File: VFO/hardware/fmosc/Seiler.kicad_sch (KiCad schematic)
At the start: 32 parts, among them J2 U.FL, J3 JST PH, J4 3670128, Q1 MMBT5179, Q2 MMBT5179, Q3 MMBT5179, Q4 MMBT5179

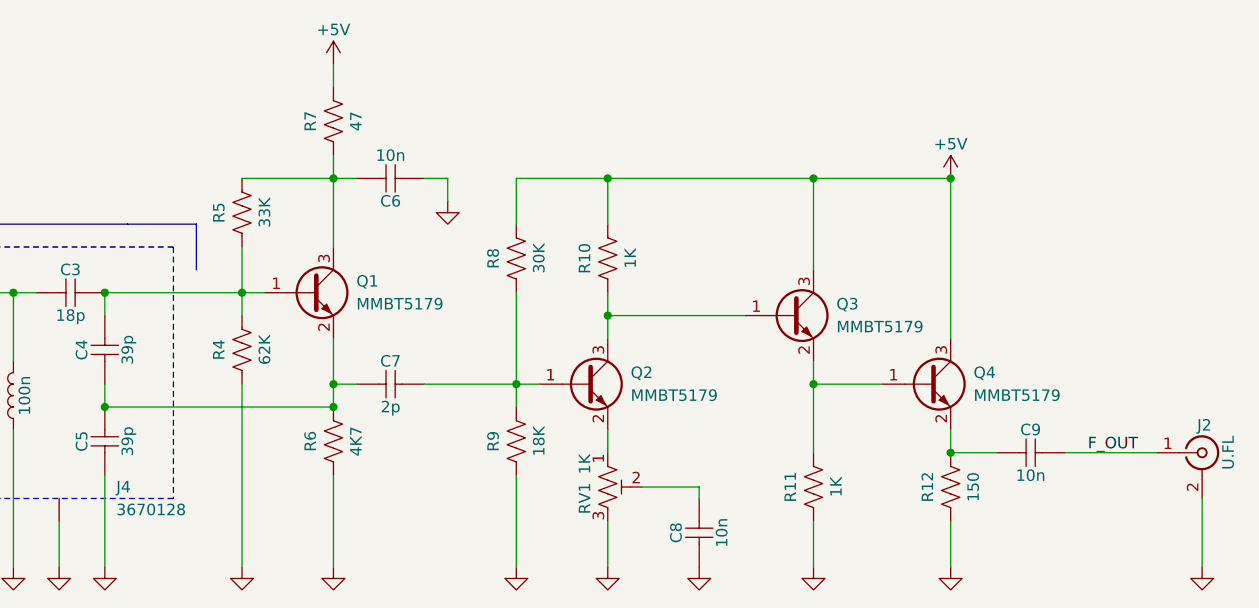
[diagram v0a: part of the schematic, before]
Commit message: Adding DC voltages to the schematic + updating from libraries
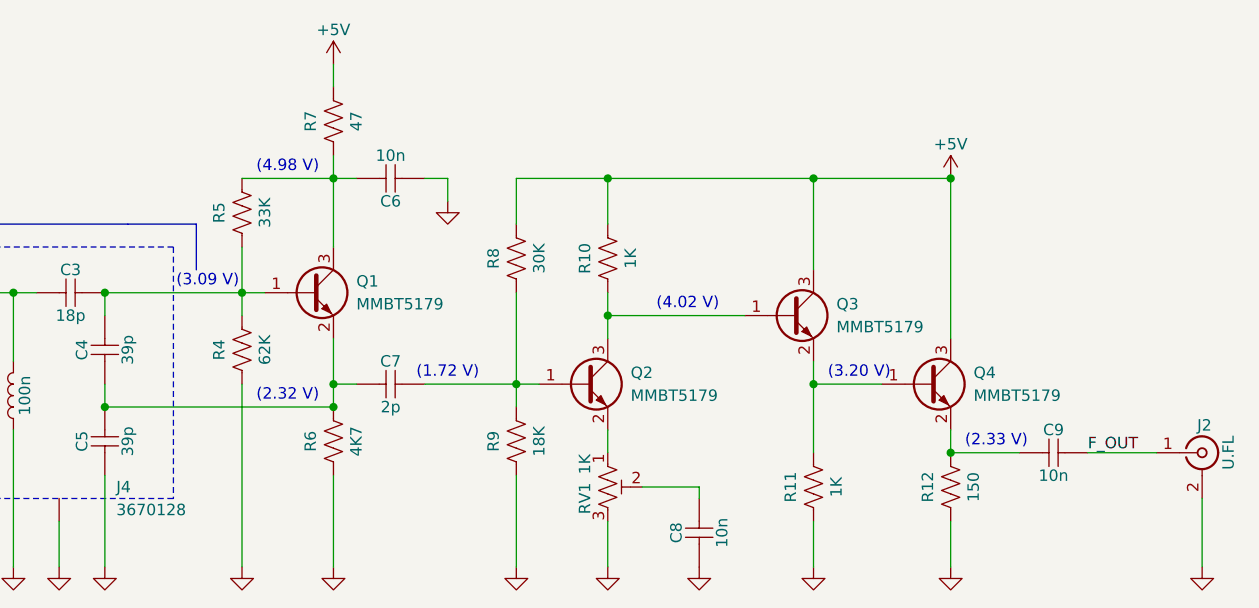
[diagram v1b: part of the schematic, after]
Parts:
- L2: symbol #gplm:ind/IND-0000-0101 -> #gplm:ind/IND-0001-0101; Current 1.7A -> 1.7; IPN IND-0000-0101 -> IND-0001-0101
- Q1, Q2, Q3, Q4: max(Ic) 50m -> 0.05
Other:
- note added: "(1.72 V)"
- note added: "(2.32 V)"
- note added: "(2.33 V)"
- note added: "(3.09 V)"
- note added: "(3.20 V)"
- note added: "(4.02 V)"
- note added: "(4.98 V)"
- moved on the sheet: C9
